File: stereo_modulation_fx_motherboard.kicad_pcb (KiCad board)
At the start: 2 copper layers, 101.6 x 139.7 mm, 64 parts, among them J1 dry_out_A, J10 Conn_01x04_Male, J11 Conn_01x02_Male, J12 Conn_01x02_Male, J2 CV_out_A, J3 wet_in_A, J4 rez_CV_out_A, J5 dry_out_B, J6 CV_out_B, J7 wet_in_B, J8 rez_CV_out_B, SW1 sweep_mode, SW2 invert_B, U1 Teensy3.2, U2 CD74HC4067M, U3 MCP4822, U4 MCP4822, U5 TL072, U6 TL072, U7 TL072, U9 CC3-0512DF-E

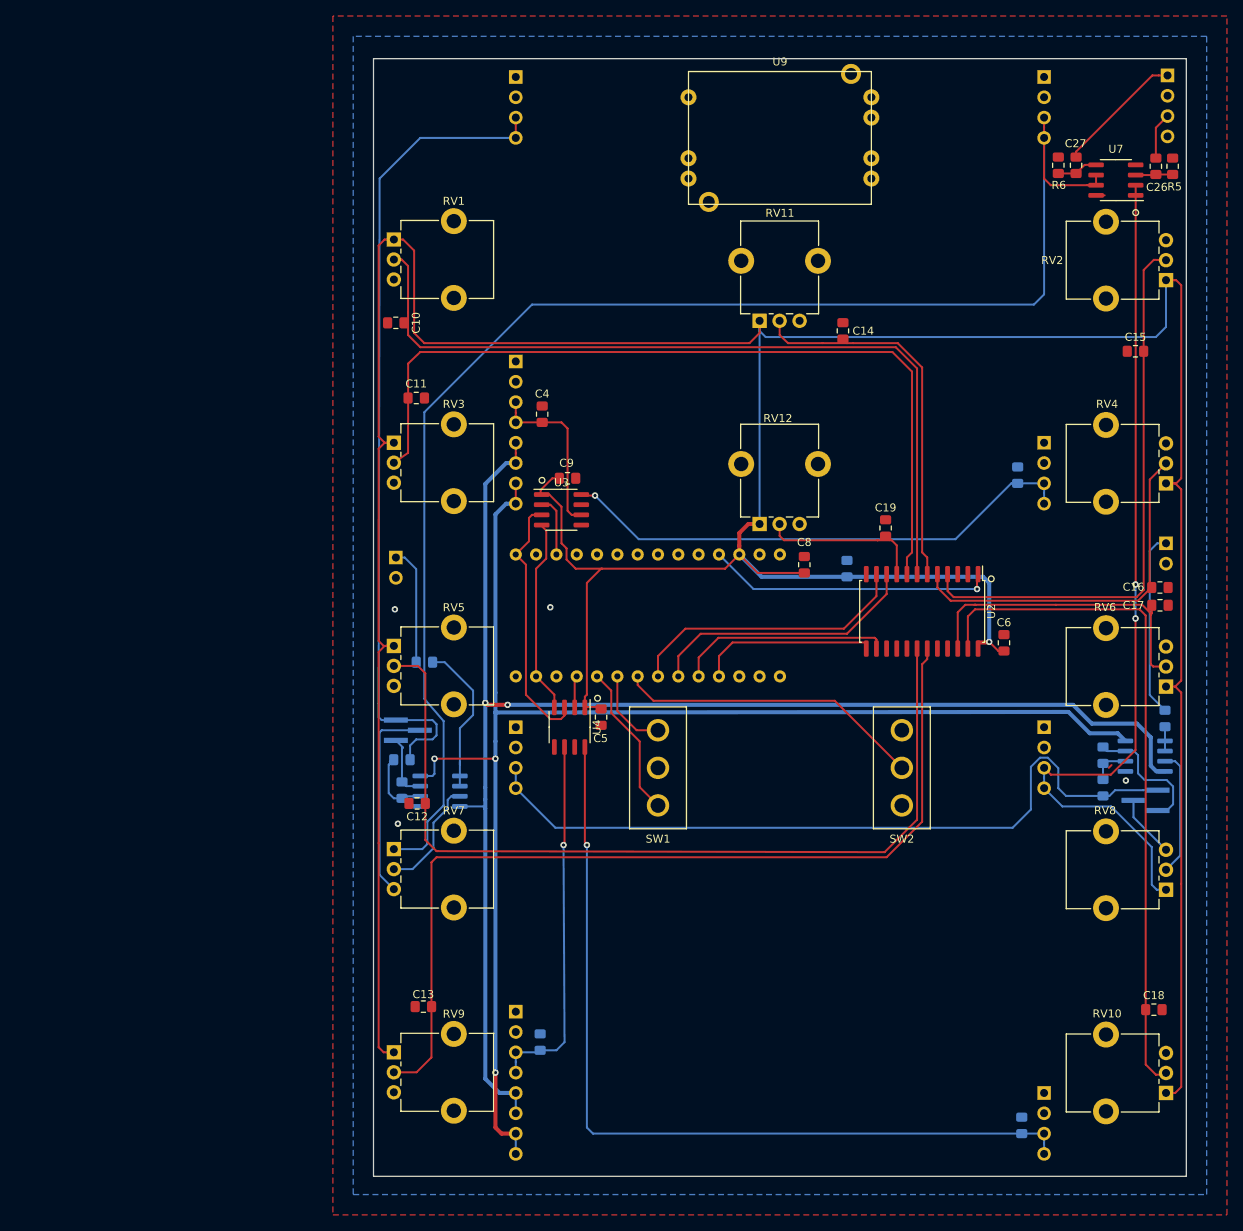
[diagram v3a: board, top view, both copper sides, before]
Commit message: remove wet/dry mixer, replace with envelope follower, NOT DONE DO NOT ORDER BOARDS!
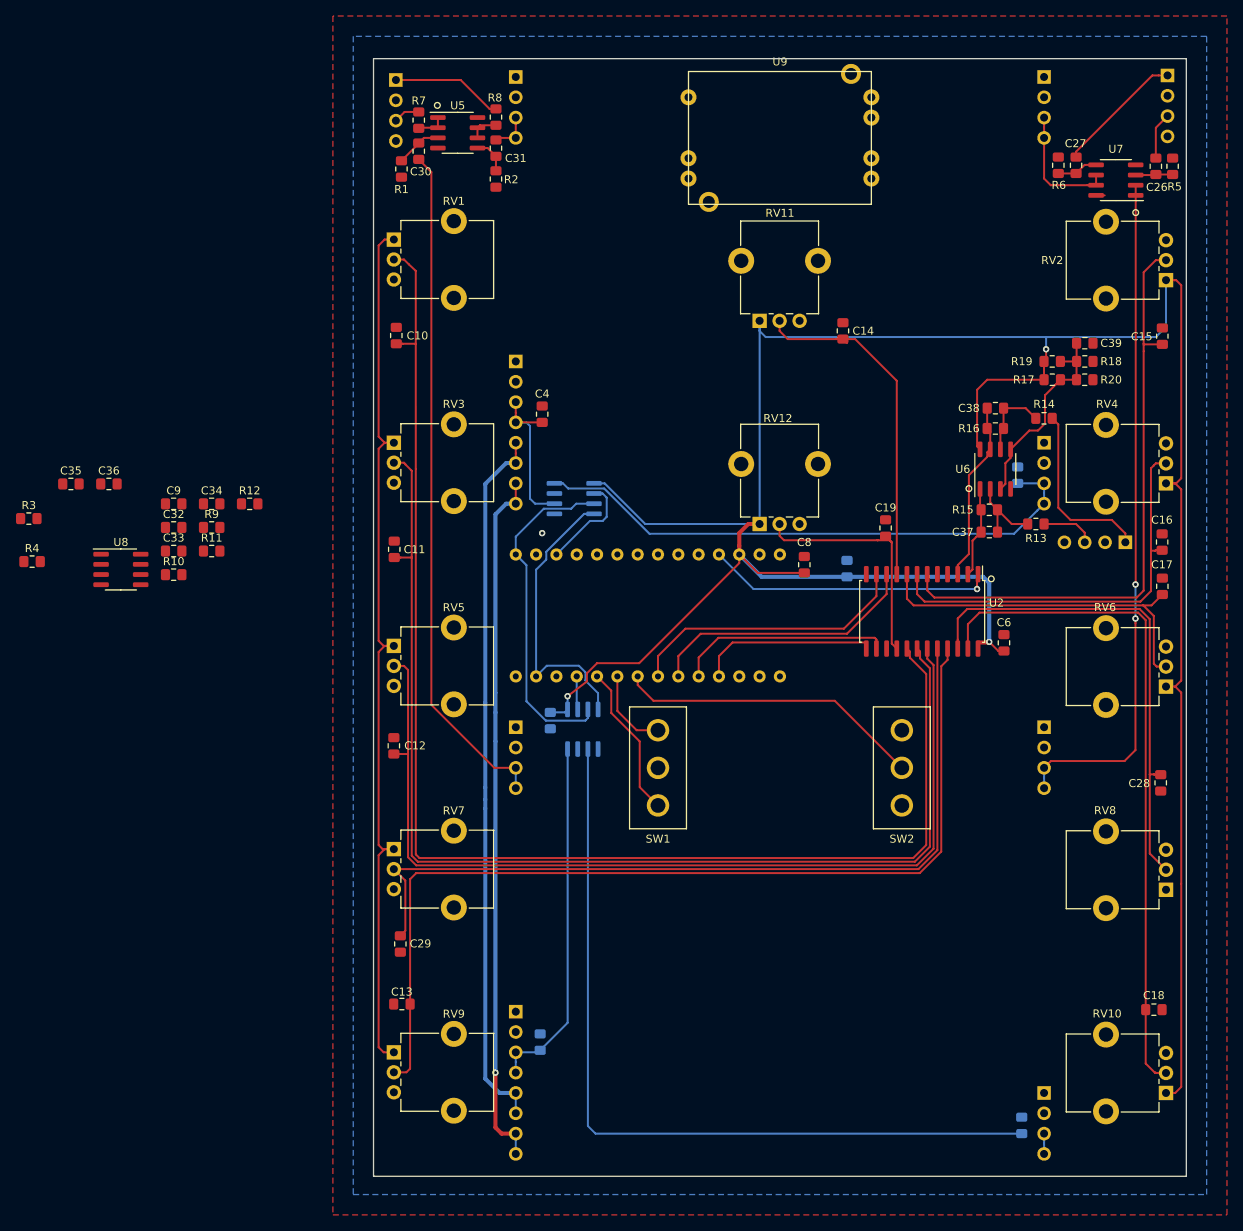
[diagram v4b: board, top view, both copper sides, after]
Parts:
- removed JP1: mix polarity A, Connector_PinHeader_1.27mm:PinHeader_1x03_P1.27mm_Vertical_SMD_Pin1Left
- removed JP2: mix polarity B, Connector_PinHeader_1.27mm:PinHeader_1x03_P1.27mm_Vertical_SMD_Pin1Left
- added C28: 100nF, Capacitor_SMD:C_0805_2012Metric_Pad1.15x1.40mm_HandSolder, F.Cu at (123.8, 116.2)
- added C29: 100nF, Capacitor_SMD:C_0805_2012Metric_Pad1.15x1.40mm_HandSolder, F.Cu at (28.8, 136.3)
- added C30: 470nF, Capacitor_SMD:C_0805_2012Metric_Pad1.15x1.40mm_HandSolder, F.Cu at (31.1, 37.2)
- added C31: 470nF, Capacitor_SMD:C_0805_2012Metric_Pad1.15x1.40mm_HandSolder, F.Cu at (40.7, 36.8)
- added C32: ???, Capacitor_SMD:C_0805_2012Metric_Pad1.15x1.40mm_HandSolder, F.Cu at (0.42, 84.3)
- added C33: ???, Capacitor_SMD:C_0805_2012Metric_Pad1.15x1.40mm_HandSolder, F.Cu at (0.42, 87.2)
- added C34: ???, Capacitor_SMD:C_0805_2012Metric_Pad1.15x1.40mm_HandSolder, F.Cu at (5.17, 81.3)
- added C35: ???, Capacitor_SMD:C_0805_2012Metric_Pad1.15x1.40mm_HandSolder, F.Cu at (-12.4, 78.8)
- added C36: ???, Capacitor_SMD:C_0805_2012Metric_Pad1.15x1.40mm_HandSolder, F.Cu at (-7.68, 78.8)
- added C37: 100nF, Capacitor_SMD:C_0805_2012Metric_Pad1.15x1.40mm_HandSolder, F.Cu at (102.4, 84.8)
- added C38: 100nF, Capacitor_SMD:C_0805_2012Metric_Pad1.15x1.40mm_HandSolder, F.Cu at (103.1, 69.3)
- added C39: 100nF, Capacitor_SMD:C_0805_2012Metric_Pad1.15x1.40mm_HandSolder, F.Cu at (114.3, 61.2)
- added R10: ???, Resistor_SMD:R_0805_2012Metric_Pad1.15x1.40mm_HandSolder, F.Cu at (0.42, 90.2)
- added R11: ???, Resistor_SMD:R_0805_2012Metric_Pad1.15x1.40mm_HandSolder, F.Cu at (5.17, 87.2)
- added R12: ???, Resistor_SMD:R_0805_2012Metric_Pad1.15x1.40mm_HandSolder, F.Cu at (9.92, 81.3)
- added R13: 12k, Resistor_SMD:R_0805_2012Metric_Pad1.15x1.40mm_HandSolder, F.Cu at (108.2, 83.8)
- added R14: 12k, Resistor_SMD:R_0805_2012Metric_Pad1.15x1.40mm_HandSolder, F.Cu at (109.2, 70.6)
- added R15: 8k2, Resistor_SMD:R_0805_2012Metric_Pad1.15x1.40mm_HandSolder, F.Cu at (102.4, 82.0)
- added R16: 8k2, Resistor_SMD:R_0805_2012Metric_Pad1.15x1.40mm_HandSolder, F.Cu at (103.1, 71.9)
- added R17: 1k5, Resistor_SMD:R_0805_2012Metric_Pad1.15x1.40mm_HandSolder, F.Cu at (110.2, 65.8)
- added R18: 2k7, Resistor_SMD:R_0805_2012Metric_Pad1.15x1.40mm_HandSolder, F.Cu at (114.3, 63.5)
- added R19: ???, Resistor_SMD:R_0805_2012Metric_Pad1.15x1.40mm_HandSolder, F.Cu at (110.2, 63.5)
- added R20: ???, Resistor_SMD:R_0805_2012Metric_Pad1.15x1.40mm_HandSolder, F.Cu at (114.3, 65.8)
- added R9: ???, Resistor_SMD:R_0805_2012Metric_Pad1.15x1.40mm_HandSolder, F.Cu at (5.17, 84.3)
- added U8: MCP6002-xSN, Package_SO:SOIC-8_3.9x4.9mm_P1.27mm, F.Cu at (-6.18, 89.5)
- C26, C27: value 47nF -> 10nF
- C5, U3, U4: moved to B.Cu
- J11, J12: value Conn_01x02_Male -> Conn_01x04_Male; footprint Connector_PinHeader_2.54mm:PinHeader_1x02_P2.54mm_Vertical -> Connector_PinHeader_2.54mm:PinHeader_1x04_P2.54mm_Vertical
- R1, R2: value 10k -> 15k; moved to F.Cu
- R3, R4: value 10k -> ???; moved to F.Cu
- R7, R8, U5: moved to F.Cu
- U6: value TL072 -> MCP6002-xSN; moved to F.Cu
- moved R3 137.5 mm to (-17.7, 83.1), turned to 0 degrees
- moved R1 116.9 mm to (28.9, 39.4)
- moved R8 112.5 mm to (40.7, 33.0)
- moved J11 112.3 mm to (28.2, 28.3)
- moved J12 91.2 mm to (119.4, 86.1), turned to 90 degrees
- moved U5 82.3 mm to (35.9, 34.9), turned to 0 degrees
- moved R2 73.5 mm to (40.7, 40.7), turned to 270 degrees
- moved R7 67.8 mm to (31.1, 33.3), turned to 270 degrees
- moved R4 54.3 mm to (-17.3, 88.5), turned to 0 degrees
- moved C9 49.3 mm to (0.42, 81.3)
- moved U6 40.5 mm to (103.1, 77.0), turned to 90 degrees
- moved C11 19.1 mm to (28.0, 87.0), turned to 90 degrees
- moved C12 7.76 mm to (27.9, 111.5), turned to 90 degrees
- moved C5 6.36 mm to (47.5, 108.4)
- moved C16 5.69 mm to (124.0, 86.1), turned to 90 degrees
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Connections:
- J11 pad 1: output_B -> output_A
- J12 pad 1: output_A -> LFO_rate_CV_in
- R1 pad 1: Net-(R1-Pad1) -> Net-(C30-Pad1)
- R1 pad 2: wet_in_B -> GNDREF
- R2 pad 1: Net-(R2-Pad1) -> Net-(C31-Pad1)
- R2 pad 2: wet_in_A -> GNDREF
- R3 pad 1: Net-(JP2-Pad3) -> Net-(C32-Pad2)
- R3 pad 2: Net-(R1-Pad1) -> Net-(C35-Pad1)
- R4 pad 1: Net-(JP1-Pad1) -> Net-(C33-Pad2)
- R4 pad 2: Net-(R2-Pad1) -> Net-(C36-Pad1)
- R7 pad 1: output_A -> output_B
- R8 pad 1: output_B -> output_A
- RV7 pad 1: dry_out_A -> +3V3
- RV7 pad 2: Net-(RV7-Pad2) -> env_B
- RV7 pad 3: Net-(JP1-Pad2) -> GNDREF
- RV8 pad 1: dry_out_B -> +3V3
- RV8 pad 2: Net-(RV8-Pad2) -> env_A
- RV8 pad 3: Net-(JP2-Pad2) -> GNDREF
- U2 pad 16: Net-(U2-Pad16) -> separation
- U2 pad 17: Net-(U2-Pad17) -> rate_A
- U2 pad 18: shape_A -> depth_A
- U2 pad 19: rez_A -> shape_A
- U2 pad 2: Net-(U2-Pad2) -> scaled_freq_CV
- U2 pad 20: Net-(U2-Pad20) -> env_B
- U2 pad 21: Net-(U2-Pad21) -> rez_A
- U2 pad 22: shape_B -> env_A
- U2 pad 3: Net-(U2-Pad3) -> scaled_LFO_rate_CV
- U2 pad 4: rate_B -> env_buff_B_out
- U2 pad 5: depth_B -> env_buff_A_out
- U2 pad 6: manual_freq -> rate_B
- U2 pad 7: rate_A -> depth_B
- U2 pad 8: depth_A -> shape_B
- U2 pad 9: separation -> manual_freq
- U3 pad 5: Net-(U3-Pad5) -> GNDREF
- U4 pad 5: Net-(U4-Pad5) -> GNDREF
- U4 pad 6: rez_CV_out_B -> CV_out_B
- U4 pad 8: CV_out_B -> rez_CV_out_B
- U5 pad 3: Net-(RV7-Pad2) -> Net-(C30-Pad1)
- U5 pad 5: GNDREF -> Net-(C31-Pad1)
- U5 pad 6: Net-(R2-Pad1) -> Net-(R8-Pad2)
- U5 pad 7: Net-(JP1-Pad1) -> Net-(R8-Pad2)
- U6 pad 1: Net-(R8-Pad2) -> scaled_freq_CV
- U6 pad 2: Net-(R8-Pad2) -> Net-(C37-Pad2)
- U6 pad 3: Net-(RV8-Pad2) -> CV_amp_bias
- U6 pad 4: -9V -> GNDREF
- U6 pad 5: GNDREF -> CV_amp_bias
- U6 pad 6: Net-(R1-Pad1) -> Net-(C38-Pad2)
- U6 pad 7: Net-(JP2-Pad3) -> scaled_LFO_rate_CV
- U6 pad 8: +9V -> +3V3
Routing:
- net dry_out_A: track 180.1 -> 16.8 mm
- net env_B: track 0.00 -> 103.3 mm
- net wet_in_A: track 103.6 -> 5.12 mm
- net -9V: track 183.0 -> 89.1 mm, vias 2 -> 0
- net +9V: track 180.4 -> 88.7 mm, vias 3 -> 1
- net rate_A: track 101.7 -> 168.9 mm
- net env_A: track 0.00 -> 62.3 mm
- net depth_A: track 102.7 -> 144.3 mm
- net +3V3: track 478.6 -> 444.3 mm, vias 1 -> 3
- net CV_amp_bias: track 0.00 -> 26.0 mm
- net Net-(JP1-Pad2): track 25.5 -> 0.00 mm
- net dry_out_B: track 109.5 -> 85.5 mm
- net scaled_LFO_rate_CV: track 0.00 -> 22.6 mm
- net LFO_rate_CV_in: track 0.00 -> 22.3 mm
- net output_B: track 23.1 -> 3.31 mm
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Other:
- board text added: "freq CV in"
- board text added: "in A"
- board text added: "in B"
- board text added: "rate CV in"
- board text removed: "A in"
- board text removed: "B in"

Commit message: continue working on layout, NOT DONE!
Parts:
- removed C5, C6, C7, C8, C9: 100nF, Capacitor_SMD:C_0805_2012Metric_Pad1.15x1.40mm_HandSolder
- added SW3: DPDT_on_on_on, stereo_modulation_fx_motherboard_custom_footprints:DPDT_on_on_on, F.Cu at (96.5, 114.3)
- C10, C11, C12, C13, C14, C15, C16, C17, C18, C19, C26, C27, C28, C29, C30, C31, C39, C4, R1, R10, R19, R2, R20, R3, R4, R5, R6, R7, R8, R9, U5, U6, U7, U8: moved to B.Cu
- C32: value ??? -> 100nF; moved to B.Cu
- C33, C34, C35, C36: value ??? -> C; moved to B.Cu
- C37, C38: value 100nF -> 4.7nF; moved to B.Cu
- R11, R12: value ??? -> 10k; moved to B.Cu
- R13, R14: value 12k -> 120k; moved to B.Cu
- R15, R16: value 8k2 -> 82k; moved to B.Cu
- R17: value 1k5 -> 15k; moved to B.Cu
- R18: value 2k7 -> 27k; moved to B.Cu
- SW1, SW2: footprint stereo_modulation_fx_motherboard_custom_footprints:NKK_M201xSS1W03 -> stereo_modulation_fx_motherboard_custom_footprints:SPDT_on_on
- moved R3 131.4 mm to (108.1, 45.0)
- moved R4 130.7 mm to (109.1, 55.2)
- moved C35 119.4 mm to (105.0, 57.5)
- moved U8 118.2 mm to (105.2, 50.1), turned to 270 degrees
- moved C36 117.4 mm to (104.0, 42.7)
- moved C33 112.7 mm to (109.1, 57.5)
- moved R10 110.3 mm to (105.0, 55.2)
- moved C34 109.9 mm to (108.1, 42.7)
- moved R9 106.4 mm to (104.0, 45.0)
- moved R11 101.3 mm to (100.4, 52.9), turned to 180 degrees
- moved C32 100.5 mm to (95.9, 52.9), turned to 180 degrees
- moved R12 89.9 mm to (95.9, 55.2), turned to 180 degrees
- moved C39 36.3 mm to (104.1, 96.1)
- moved R19 31.9 mm to (100.0, 93.8)
- moved R18 31.9 mm to (104.1, 93.8)
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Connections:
- C1 pad 2: GNDREF -> GNDA
- C10 pad 2: GNDREF -> GNDA
- C11 pad 2: GNDREF -> GNDA
- C12 pad 2: GNDREF -> GNDA
- C13 pad 2: GNDREF -> GNDA
- C14 pad 2: GNDREF -> GNDA
- C15 pad 2: GNDREF -> GNDA
- C16 pad 2: GNDREF -> GNDA
- C17 pad 2: GNDREF -> GNDA
- C18 pad 2: GNDREF -> GNDA
- C19 pad 2: GNDREF -> GNDA
- C2 pad 2: GNDREF -> GNDA
- C26 pad 2: input_B -> input_A
- C27 pad 2: input_A -> input_B
- C28 pad 2: GNDREF -> GNDA
- C29 pad 2: GNDREF -> GNDA
- C3 pad 2: GNDREF -> GNDA
- C30 pad 2: wet_in_B -> wet_A
- C31 pad 2: wet_in_A -> wet_B
- C32 pad 1: env_buff_A_out -> audio_to_uC_amp_bias
- C32 pad 2: Net-(C32-Pad2) -> GNDA
- C33 pad 1: env_buff_B_out -> Net-(C33-Pad1)
- C33 pad 2: Net-(C33-Pad2) -> dry_B
- C34 pad 1: env_bias -> Net-(C34-Pad1)
- C34 pad 2: GNDREF -> dry_A
- C35 pad 1: Net-(C35-Pad1) -> B_to_uC
- C35 pad 2: dry_out_A -> Net-(C35-Pad2)
- C36 pad 1: Net-(C36-Pad1) -> A_to_uC
- C36 pad 2: dry_out_B -> Net-(C36-Pad2)
- C37 pad 1: scaled_freq_CV -> scaled_LFO_rate_CV
- C38 pad 1: scaled_LFO_rate_CV -> scaled_freq_CV
- C39 pad 2: GNDREF -> GNDA
- C4 pad 2: GNDREF -> GNDA
- J1 pad 1: GNDREF -> GNDA
- J1 pad 2: GNDREF -> GNDA
- J1 pad 3: dry_out_A -> dry_A
- J1 pad 4: dry_out_A -> dry_A
- J10 pad 2: GNDREF -> GNDA
- J10 pad 4: GNDREF -> GNDA
- J11 pad 2: GNDREF -> GNDA
- J11 pad 4: GNDREF -> GNDA
- J12 pad 2: GNDREF -> GNDA
- J12 pad 4: GNDREF -> GNDA
- J2 pad 1: GNDREF -> GNDA
- J2 pad 2: GNDREF -> GNDA
- J3 pad 1: GNDREF -> GNDA
- J3 pad 2: GNDREF -> GNDA
- J3 pad 3: wet_in_A -> wet_A
- J3 pad 4: wet_in_A -> wet_A
- J4 pad 1: GNDREF -> GNDA
- J4 pad 2: GNDREF -> GNDA
- J5 pad 1: GNDREF -> GNDA
- J5 pad 2: GNDREF -> GNDA
- J5 pad 3: dry_out_B -> dry_B
- J5 pad 4: dry_out_B -> dry_B
- J6 pad 1: GNDREF -> GNDA
- J6 pad 2: GNDREF -> GNDA
- J7 pad 1: GNDREF -> GNDA
- J7 pad 2: GNDREF -> GNDA
- J7 pad 3: wet_in_B -> wet_B
- J7 pad 4: wet_in_B -> wet_B
- J8 pad 1: GNDREF -> GNDA
- J8 pad 2: GNDREF -> GNDA
- R1 pad 2: GNDREF -> GNDA
- R10 pad 1: env_buff_B_out -> B_to_uC
- R10 pad 2: Net-(C33-Pad2) -> Net-(C35-Pad2)
- R11 pad 2: env_bias -> audio_to_uC_amp_bias
- R12 pad 1: env_bias -> audio_to_uC_amp_bias
- R12 pad 2: GNDREF -> GNDA
- R13 pad 1: Net-(C37-Pad2) -> Net-(C38-Pad2)
- R14 pad 1: Net-(C38-Pad2) -> Net-(C37-Pad2)
- R15 pad 1: scaled_freq_CV -> scaled_LFO_rate_CV
- R16 pad 1: scaled_LFO_rate_CV -> scaled_freq_CV
- R18 pad 2: GNDREF -> GNDA
- R2 pad 2: GNDREF -> GNDA
- R20 pad 2: GNDREF -> GNDA
- R3 pad 1: Net-(C32-Pad2) -> Net-(C36-Pad2)
- R3 pad 2: Net-(C35-Pad1) -> Net-(C34-Pad1)
- R4 pad 1: Net-(C33-Pad2) -> Net-(C35-Pad2)
- R4 pad 2: Net-(C36-Pad1) -> Net-(C33-Pad1)
- R5 pad 2: GNDREF -> GNDA
- R6 pad 2: GNDREF -> GNDA
- R7 pad 1: output_B -> output_A
- R8 pad 1: output_A -> output_B
- R9 pad 1: env_buff_A_out -> A_to_uC
- R9 pad 2: Net-(C32-Pad2) -> Net-(C36-Pad2)
- RV1 pad 3: GNDREF -> GNDA
- RV10 pad 3: GNDREF -> GNDA
- RV11 pad 3: GNDREF -> GNDA
- RV12 pad 3: GNDREF -> GNDA
- RV2 pad 3: GNDREF -> GNDA
- RV3 pad 3: GNDREF -> GNDA
- RV4 pad 3: GNDREF -> GNDA
- RV5 pad 3: GNDREF -> GNDA
- RV6 pad 3: GNDREF -> GNDA
- RV7 pad 3: GNDREF -> GNDA
- RV8 pad 3: GNDREF -> GNDA
- RV9 pad 3: GNDREF -> GNDA
- SW1 pad 2: GNDREF -> GNDA
- SW2 pad 1: Net-(SW2-Pad1) -> inv_B_switch
- SW2 pad 2: inv_B_switch -> GNDA
- SW2 pad 3: GNDREF -> Net-(SW2-Pad3)
- U1 pad 1: GNDREF -> GNDA
- U1 pad 32: GNDREF -> GNDA
- U2 pad 12: GNDREF -> GNDA
- U2 pad 15: GNDREF -> GNDA
- U2 pad 22: env_A -> rez_B
- U2 pad 23: rez_B -> env_A
- U2 pad 4: env_buff_B_out -> B_to_uC
- U2 pad 5: env_buff_A_out -> A_to_uC
- U3 pad 5: GNDREF -> GNDA
- U3 pad 7: GNDREF -> GNDA
- U4 pad 5: GNDREF -> GNDA
- U4 pad 7: GNDREF -> GNDA
- U6 pad 1: scaled_freq_CV -> scaled_LFO_rate_CV
- U6 pad 4: GNDREF -> GNDA
- U6 pad 7: scaled_LFO_rate_CV -> scaled_freq_CV
- U7 pad 1: dry_out_B -> dry_A
- U7 pad 2: dry_out_B -> dry_A
- U7 pad 6: dry_out_A -> Net-(SW3-Pad6)
- U7 pad 7: dry_out_A -> Net-(SW3-Pad6)
- U8 pad 1: env_buff_A_out -> A_to_uC
- U8 pad 2: Net-(C32-Pad2) -> Net-(C36-Pad2)
- U8 pad 3: env_bias -> audio_to_uC_amp_bias
- U8 pad 4: GNDREF -> GNDA
- U8 pad 5: env_bias -> audio_to_uC_amp_bias
- U8 pad 6: Net-(C33-Pad2) -> Net-(C35-Pad2)
- U8 pad 7: env_buff_B_out -> B_to_uC
- U9 pad 5: GNDREF -> GNDA
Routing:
- net wet_A: track 0.00 -> 178.4 mm, vias 0 -> 1
- net GNDA: track 0.00 -> 138.1 mm, vias 0 -> 1
- net dry_A: track 0.00 -> 133.7 mm
- net Net-(SW3-Pad6): track 0.00 -> 128.9 mm
- net +3V3: track 444.3 -> 556.6 mm
- net dry_out_B: track 85.5 -> 0.00 mm, vias 2 -> 0
- net wet_in_B: track 85.2 -> 0.00 mm
- net wet_B: track 0.00 -> 80.2 mm, vias 0 -> 1
- net dry_B: track 0.00 -> 79.5 mm
- net B_to_uC: track 0.00 -> 74.9 mm, vias 0 -> 1
- net A_to_uC: track 0.00 -> 54.3 mm, vias 0 -> 1
- net audio_to_uC_amp_bias: track 0.00 -> 18.5 mm
- net env_A: track 62.3 -> 44.3 mm
- net inv_B_switch: track 38.4 -> 20.6 mm
- net dry_out_A: track 16.8 -> 0.00 mm
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- added copper zone on B.Cu, net GNDA
- added copper zone on F.Cu, net GNDA
- removed copper zone on B.Cu, net GNDREF
- removed copper zone on F.Cu, net GNDREF

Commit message: move all components to one side of board, play with trace layout, NOT DONEgit add -A!
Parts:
- added J13: Conn_01x02_Male, Connector_PinHeader_2.54mm:PinHeader_1x02_P2.54mm_Vertical, B.Cu at (119.8, 161.9)
- added J14: Conn_01x02_Male, Connector_PinHeader_2.54mm:PinHeader_1x02_P2.54mm_Vertical, B.Cu at (32.6, 162.1)
- added U10: DG419LDY, Package_SO:SOIC-8_3.9x4.9mm_P1.27mm, B.Cu at (48.6, 45.8)
- added U11: DG419LDY, Package_SO:SOIC-8_3.9x4.9mm_P1.27mm, B.Cu at (41.1, 45.8)
- U2, U9: moved to B.Cu
- moved U9 113.9 mm to (71.8, 149.4)
- moved RV7 96.7 mm to (124.5, 129.5), turned to 180 degrees
- moved RV8 96.7 mm to (27.9, 124.5), turned to 0 degrees
- moved C28 91.9 mm to (30.4, 128.3), turned to 270 degrees
- moved C29 91.7 mm to (122.0, 125.7), turned to 90 degrees
- moved C39 22.5 mm to (90.6, 78.1), turned to 180 degrees
- moved C32 20.7 mm to (83.4, 69.4)
- moved R12 20.7 mm to (83.4, 71.7)
- moved U8 20.7 mm to (92.8, 66.6)
- moved C36 20.7 mm to (91.6, 59.2)
- moved R9 20.7 mm to (91.6, 61.5)
- moved C33 20.7 mm to (96.6, 74.0)
- moved C35 20.7 mm to (92.6, 74.0)
- moved R11 20.7 mm to (88.0, 69.4)
- moved C34 20.7 mm to (95.6, 59.2)
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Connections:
- net +9V renamed +12V
- net -9V renamed -12V
- C30 pad 2: wet_A -> Net-(C30-Pad2)
- C31 pad 2: wet_B -> Net-(C31-Pad2)
- U1 pad 24: Net-(U1-Pad24) -> bypass_B
- U1 pad 25: Net-(U1-Pad25) -> bypass_A
- U1 pad 26: Net-(U1-Pad26) -> mux_S1
- U1 pad 27: Net-(U1-Pad27) -> mux_S0
- U1 pad 28: Net-(U1-Pad28) -> muxed_pots
- U1 pad 29: Net-(U1-Pad29) -> mux_S2
- U1 pad 30: muxed_pots -> mux_S3
- U1 pad 4: mux_S3 -> Net-(U1-Pad4)
- U1 pad 5: mux_S2 -> Net-(U1-Pad5)
- U1 pad 6: mux_S0 -> footswitch_A
- U1 pad 7: mux_S1 -> footswitch_B
- U2 pad 17: rate_A -> manual_freq
- U2 pad 18: depth_A -> depth_B
- U2 pad 19: shape_A -> rate_B
- U2 pad 2: scaled_freq_CV -> shape_B
- U2 pad 20: env_B -> A_to_uC
- U2 pad 21: rez_A -> B_to_uC
- U2 pad 22: rez_B -> scaled_freq_CV
- U2 pad 23: env_A -> scaled_LFO_rate_CV
- U2 pad 3: scaled_LFO_rate_CV -> env_B
- U2 pad 4: B_to_uC -> rez_B
- U2 pad 5: A_to_uC -> rez_A
- U2 pad 6: rate_B -> env_A
- U2 pad 7: depth_B -> shape_A
- U2 pad 8: shape_B -> depth_A
- U2 pad 9: manual_freq -> rate_A
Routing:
- net +3V3: track 556.6 -> 490.1 mm
- net dry_A: track 133.7 -> 185.1 mm, vias 0 -> 3
- net bypass_B: track 0.00 -> 49.8 mm, vias 0 -> 1
- net bypass_A: track 0.00 -> 45.6 mm, vias 0 -> 1
- net env_A: track 44.3 -> 88.8 mm, vias 0 -> 2
- net Net-(SW3-Pad6): track 128.9 -> 170.8 mm, vias 0 -> 2
- net wet_A: track 178.4 -> 141.8 mm, vias 1 -> 2
- net env_B: track 95.1 -> 59.2 mm, vias 0 -> 2
- net GNDA: track 138.1 -> 165.4 mm, vias 1 -> 4
- net Net-(C30-Pad2): track 0.00 -> 25.7 mm, vias 0 -> 2
- net dry_B: track 79.5 -> 54.1 mm, vias 0 -> 1
- net A_to_uC: track 54.3 -> 31.5 mm, vias 1 -> 2
- net B_to_uC: track 74.9 -> 53.3 mm, vias 1 -> 2
- net rez_B: track 68.8 -> 86.6 mm, vias 0 -> 3
- net separation: track 36.4 -> 21.3 mm, vias 0 -> 2
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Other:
- board text removed: "out A"
- board text removed: "out B"
